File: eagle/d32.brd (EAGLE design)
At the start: 61.7 x 39.8 mm, 4 parts

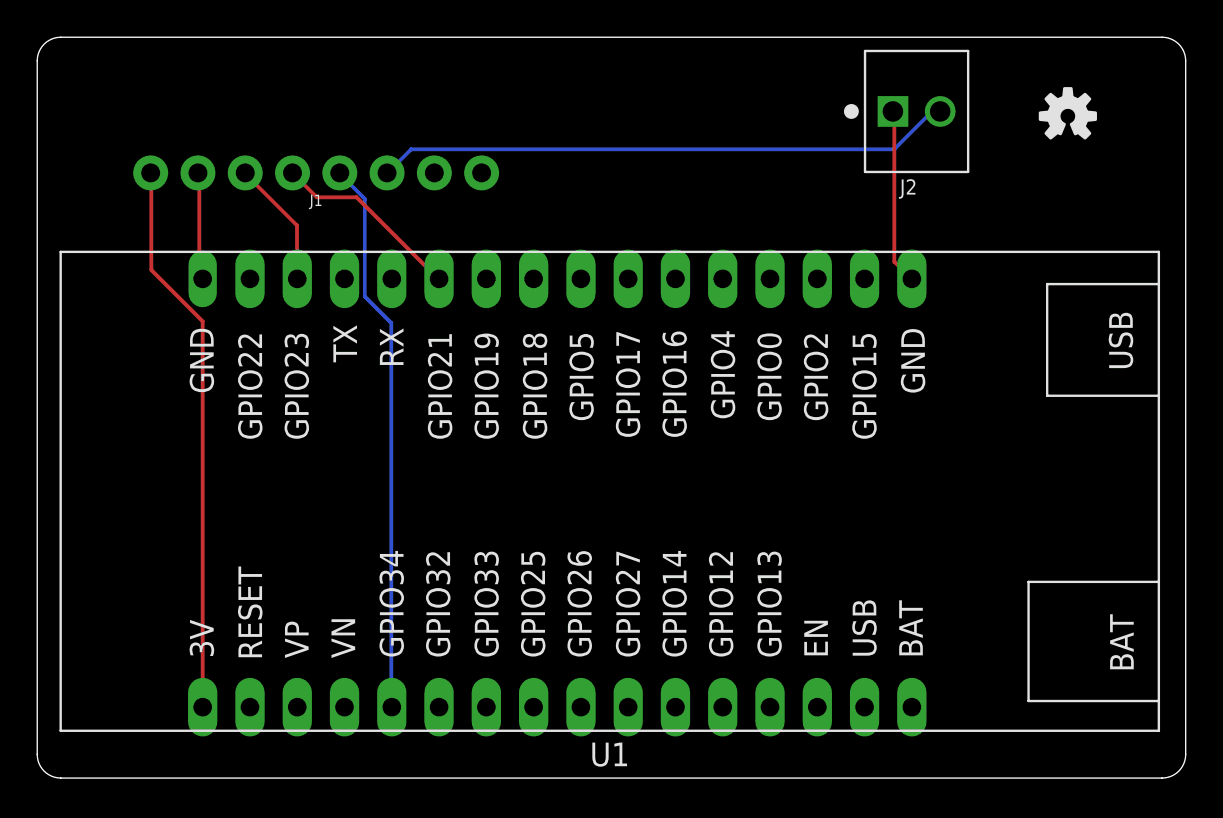
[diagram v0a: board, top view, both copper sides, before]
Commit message: sync boards to use same net classes, update images with new traces
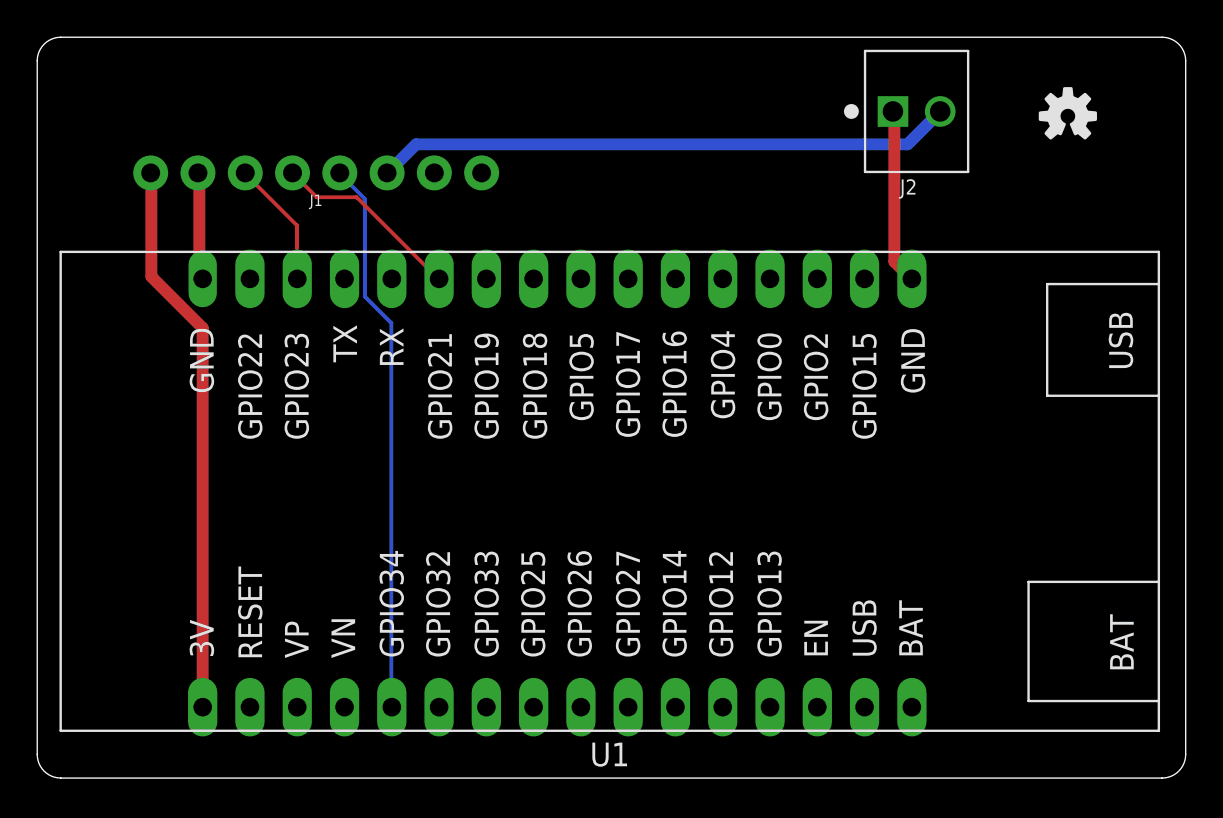
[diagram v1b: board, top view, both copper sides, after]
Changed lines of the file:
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@@
 </variantdefs>
 <classes>
-<class number="0" name="default" width="0" drill="0">
+<class number="0" name="default" width="0.1524" drill="0">
 <clearance class="0" value="0.1524"/>
+</class>
+<class number="1" name="current" width="0.635" drill="0">
 </class>
 <class number="2" name="signal" width="0.2032" drill="0">
@@
 <wire x1="16.2687" y1="32.4485" x2="16.256" y2="32.512" width="0.2032" layer="16"/>
 </signal>
-<signal name="VBUS" class="2">
+<signal name="VBUS" class="1">
 <contactref element="J2" pad="2"/>
 <contactref element="J1" pad="6"/>
-<wire x1="48.006" y1="35.7378" x2="48.4505" y2="35.7378" width="0.2032" layer="16"/>
-<wire x1="46.0502" y1="33.782" x2="48.006" y2="35.7378" width="0.2032" layer="16"/>
-<wire x1="20.0914" y1="33.782" x2="46.0502" y2="33.782" width="0.2032" layer="16"/>
-<wire x1="18.8468" y1="32.5374" x2="20.0914" y2="33.782" width="0.2032" layer="16"/>
-<wire x1="48.4505" y1="35.7378" x2="48.514" y2="35.814" width="0.2032" layer="16"/>
-<wire x1="18.8468" y1="32.5374" x2="18.796" y2="32.512" width="0.2032" layer="16"/>
-</signal>
-<signal name="3.3V" class="2">
+<wire x1="46.7614" y1="34.0487" x2="48.4505" y2="35.7378" width="0.635" layer="16"/>
+<wire x1="20.3581" y1="34.0487" x2="46.7614" y2="34.0487" width="0.635" layer="16"/>
+<wire x1="18.8468" y1="32.5374" x2="20.3581" y2="34.0487" width="0.635" layer="16"/>
+<wire x1="48.4505" y1="35.7378" x2="48.514" y2="35.814" width="0.635" layer="16"/>
+<wire x1="18.8468" y1="32.5374" x2="18.796" y2="32.512" width="0.635" layer="16"/>
+</signal>
+<signal name="3.3V" class="1">
 <contactref element="U1" pad="1"/>
 <contactref element="J1" pad="1"/>
-<wire x1="8.89" y1="24.5364" x2="8.89" y2="3.81" width="0.2032" layer="1"/>
-<wire x1="6.1341" y1="27.2923" x2="8.89" y2="24.5364" width="0.2032" layer="1"/>
-<wire x1="6.1341" y1="32.4485" x2="6.1341" y2="27.2923" width="0.2032" layer="1"/>
-<wire x1="6.1341" y1="32.4485" x2="6.096" y2="32.512" width="0.2032" layer="1"/>
-</signal>
-<signal name="GND" class="2">
+<wire x1="8.89" y1="24.1808" x2="8.89" y2="3.81" width="0.635" layer="1"/>
+<wire x1="6.1341" y1="26.9367" x2="8.89" y2="24.1808" width="0.635" layer="1"/>
+<wire x1="6.1341" y1="32.4485" x2="6.1341" y2="26.9367" width="0.635" layer="1"/>
+<wire x1="6.1341" y1="32.4485" x2="6.096" y2="32.512" width="0.635" layer="1"/>
+</signal>
+<signal name="GND" class="1">
 <contactref element="U1" pad="17" route="any" routetag="G$1.GND"/>
 <contactref element="U1" pad="32" route="any" routetag="G$1.GND"/>
 <contactref element="J2" pad="1"/>
 <contactref element="J1" pad="2"/>
-<wire x1="46.0502" y1="27.7368" x2="46.0502" y2="35.7378" width="0.2032" layer="1"/>
-<wire x1="46.9392" y1="26.8478" x2="46.0502" y2="27.7368" width="0.2032" layer="1"/>
-<wire x1="46.0502" y1="35.7378" x2="45.974" y2="35.814" width="0.2032" layer="1"/>
-<wire x1="46.9392" y1="26.8478" x2="46.99" y2="26.82" width="0.2032" layer="1"/>
-<wire x1="8.7122" y1="27.0256" x2="8.7122" y2="32.4485" width="0.2032" layer="1"/>
-<wire x1="8.89" y1="26.8478" x2="8.7122" y2="27.0256" width="0.2032" layer="1"/>
-<wire x1="8.7122" y1="32.4485" x2="8.636" y2="32.512" width="0.2032" layer="1"/>
-<wire x1="8.89" y1="26.8478" x2="8.89" y2="26.82" width="0.2032" layer="1"/>
+<wire x1="46.0502" y1="27.7368" x2="46.0502" y2="35.7378" width="0.635" layer="1"/>
+<wire x1="46.9392" y1="26.8478" x2="46.0502" y2="27.7368" width="0.635" layer="1"/>
+<wire x1="46.0502" y1="35.7378" x2="45.974" y2="35.814" width="0.635" layer="1"/>
+<wire x1="46.9392" y1="26.8478" x2="46.99" y2="26.82" width="0.635" layer="1"/>
+<wire x1="8.7122" y1="27.0256" x2="8.7122" y2="32.4485" width="0.635" layer="1"/>
+<wire x1="8.89" y1="26.8478" x2="8.7122" y2="27.0256" width="0.635" layer="1"/>
+<wire x1="8.7122" y1="32.4485" x2="8.636" y2="32.512" width="0.635" layer="1"/>
+<wire x1="8.89" y1="26.8478" x2="8.89" y2="26.82" width="0.635" layer="1"/>
 </signal>
 </signals>
